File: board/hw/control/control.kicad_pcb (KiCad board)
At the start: 2 copper layers, 54.3 x 82.5 mm, 45 parts, among them J1 stepper #1, J2 stepper #2, J3 buttons, J4 power, J6 AVR-ISP-10, Q1 MMFTP84W, Q2 MMFTP84W, U1 ULN2003A, U2 ULN2003A, U3 ULN2003A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

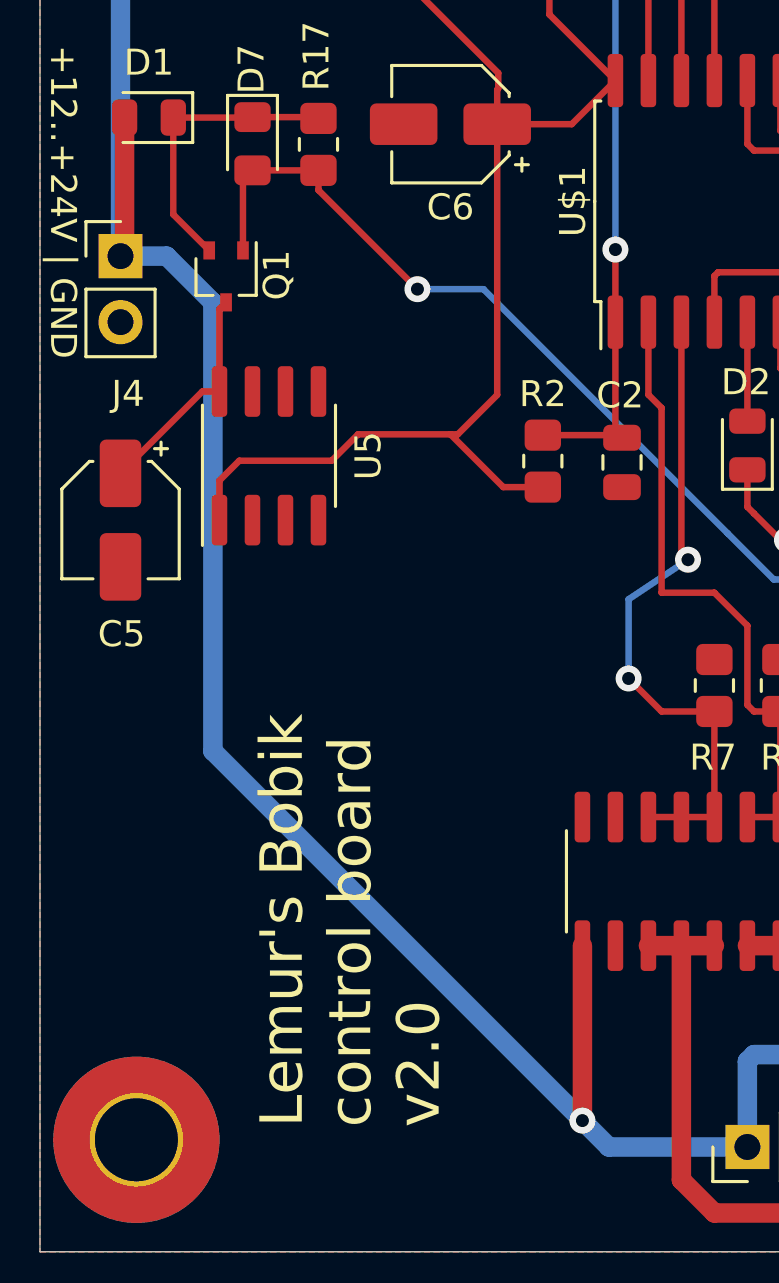
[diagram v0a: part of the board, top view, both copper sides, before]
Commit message: added power-on LED to +5V line
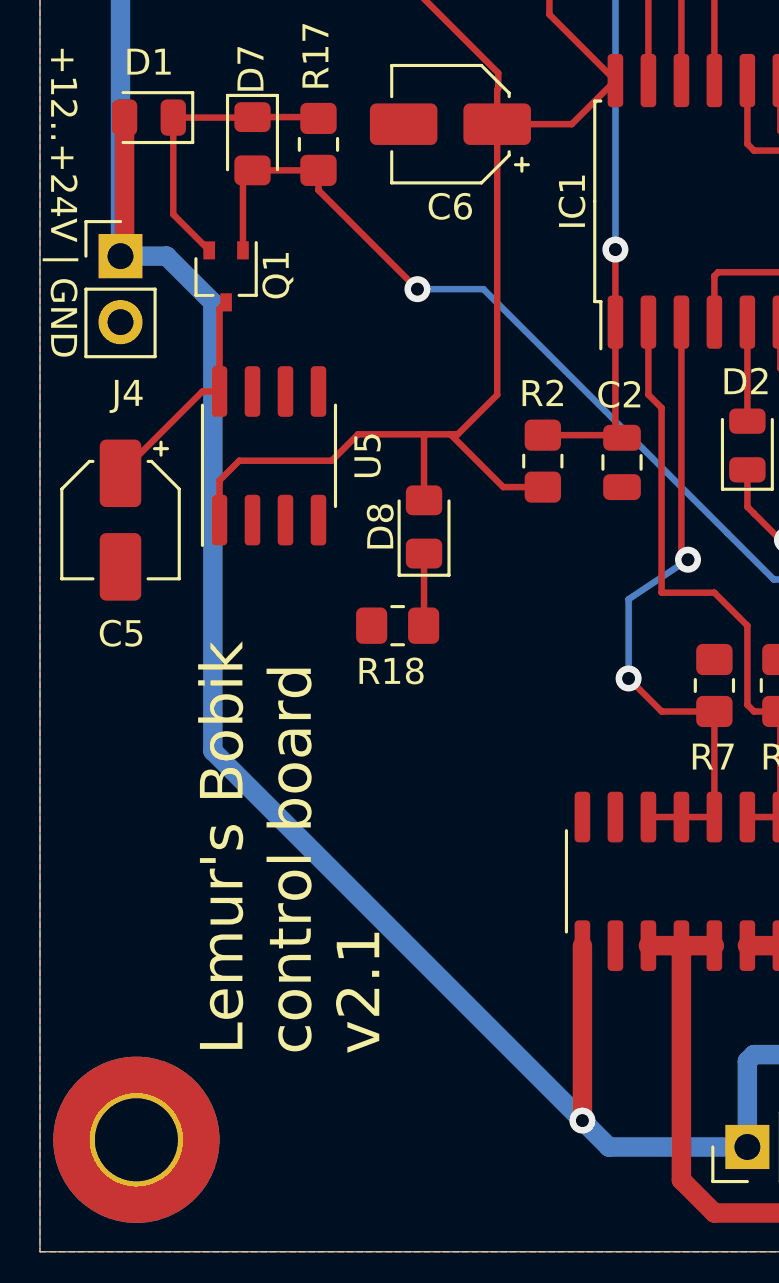
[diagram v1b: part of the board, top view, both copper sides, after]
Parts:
- added D8: LED green, LED_SMD:LED_0805_2012Metric_Pad1.15x1.40mm_HandSolder, F.Cu at (136.1, 118.4)
- added R18: 1kR, Resistor_SMD:R_0805_2012Metric_Pad1.20x1.40mm_HandSolder, F.Cu at (135.1, 122.2)
- renumbered U$1 to IC1
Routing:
- net Net-(D8-K): track 0.00 -> 2.78 mm
- net +5V: track 60.1 -> 62.7 mm
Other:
- board text added: "Lemur's Bobik control board v2.1"
- board text removed: "Lemur's Bobik control board v2.0"

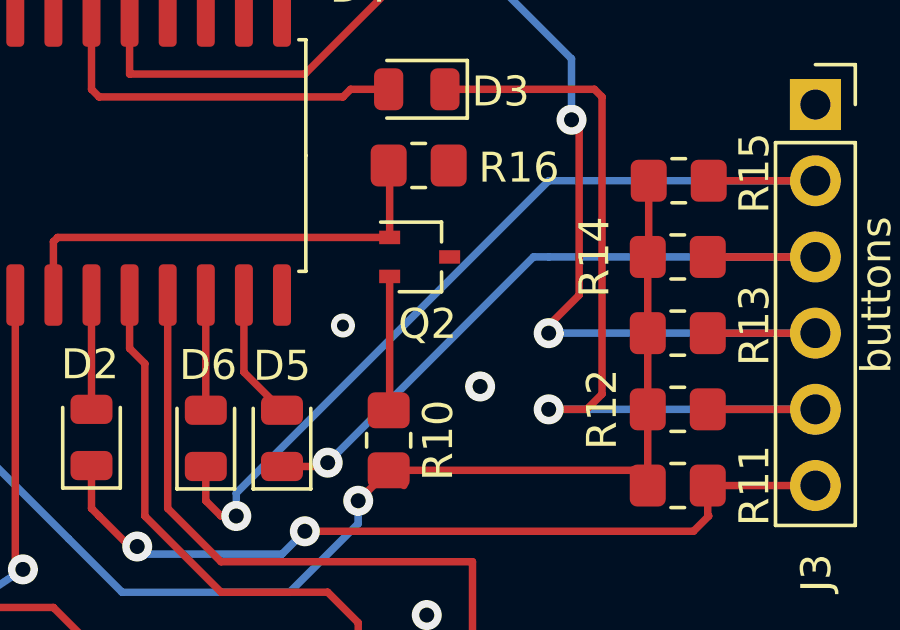
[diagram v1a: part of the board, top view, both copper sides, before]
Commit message: replaced P-MOSFET with N-MOSFET to maintain power-on state
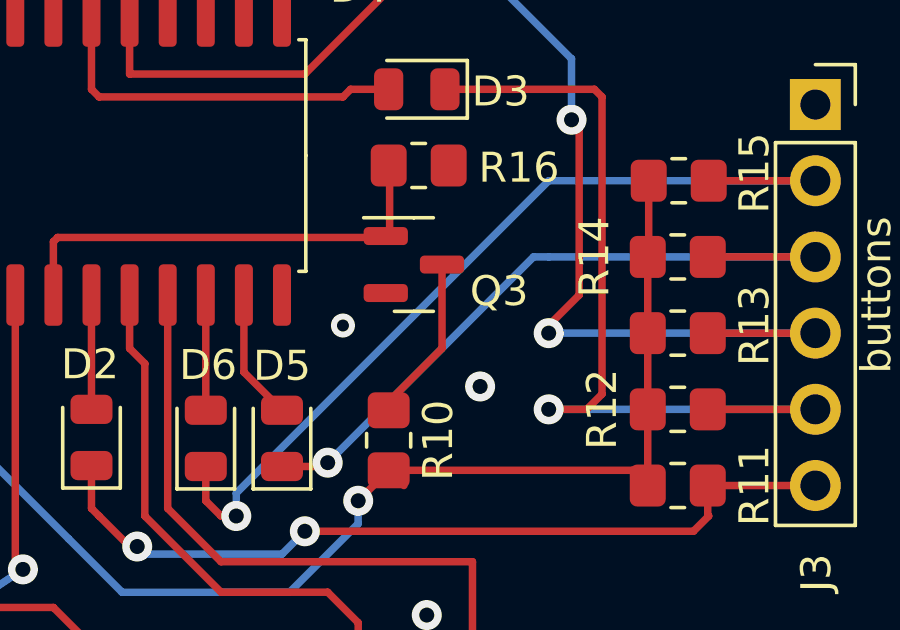
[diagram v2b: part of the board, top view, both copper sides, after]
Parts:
- removed Q2: MMFTP84W, Package_TO_SOT_SMD:SOT-323_SC-70
- added Q3: 2N7002, Package_TO_SOT_SMD:SOT-23, F.Cu at (159.3, 109.5)
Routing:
- net Net-(Q3-D): track 4.48 -> 5.64 mm

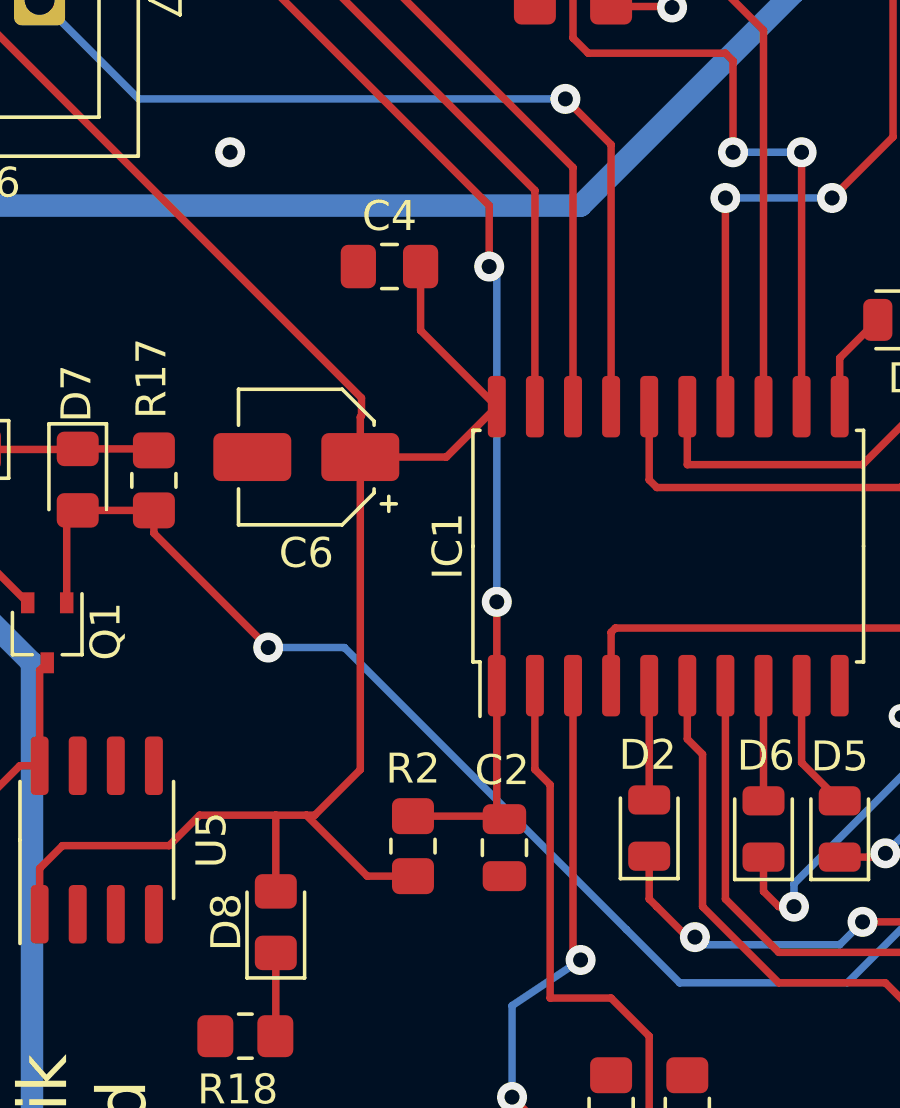
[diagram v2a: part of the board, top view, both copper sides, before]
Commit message: C2 and C4 are not 1206 as they should
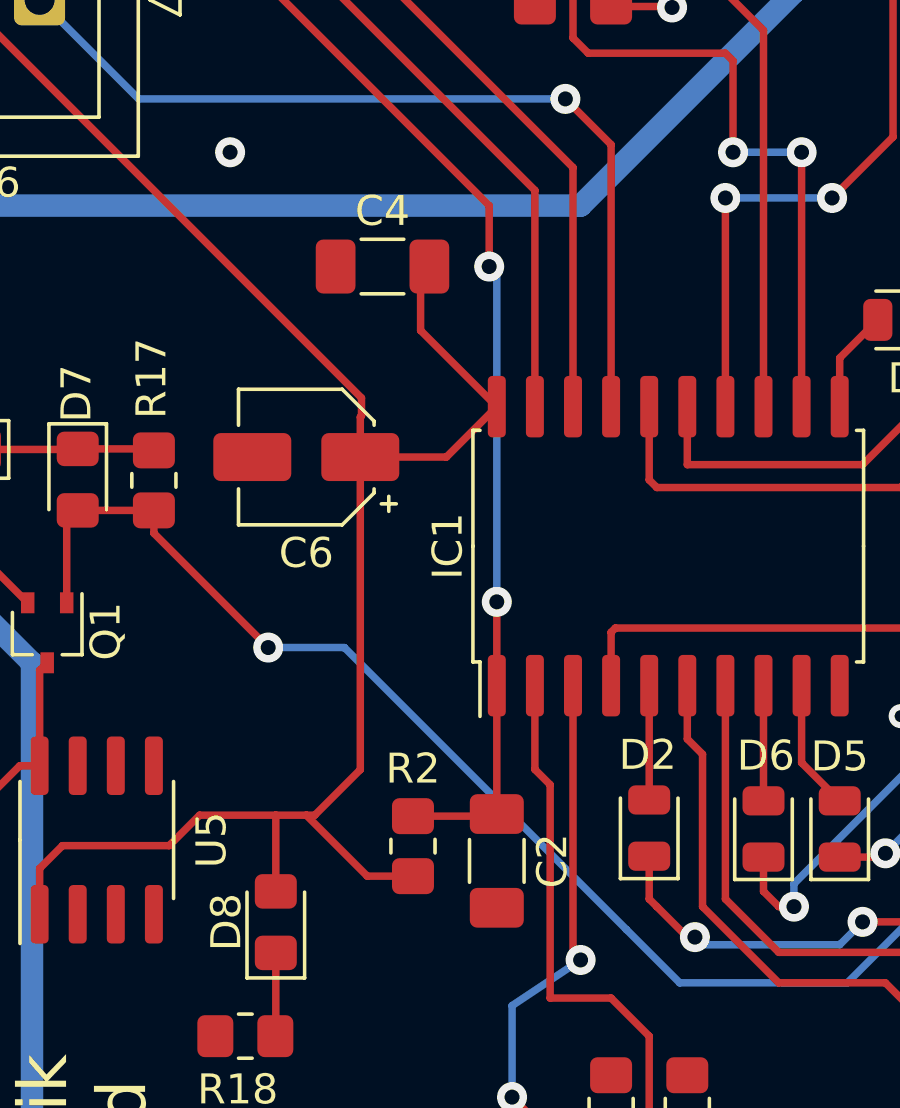
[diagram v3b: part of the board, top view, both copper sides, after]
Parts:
- C2: footprint Capacitor_SMD:C_0805_2012Metric -> Capacitor_SMD:C_1206_3216Metric_Pad1.33x1.80mm_HandSolder
- C4: footprint Capacitor_SMD:C_0805_2012Metric_Pad1.18x1.45mm_HandSolder -> Capacitor_SMD:C_1206_3216Metric_Pad1.33x1.80mm_HandSolder
- moved C2 0.51 mm to (143.5, 116.3)
- moved C4 0.23 mm to (139.7, 96.5)
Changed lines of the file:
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@@
     (pad "1" connect circle (at 0 0) (size 6.4 6.4) (layers "B.Cu" "B.Mask"))
   )
-  (footprint "Capacitor_SMD:C_0805_2012Metric" (layer "F.Cu")
-    (at 143.764 115.89 -90)
-    (descr "Capacitor SMD 0805 (2012 Metric), square (rectangular) end terminal, IPC_7351 nominal, (Body size source: IPC-SM-782 page 76, https://www.pcb-3d.com/wordpress/wp-content/uploads/ipc-sm-782a_amendment_1_and_2.pdf, https://docs.google.com/spreadsheets/d/1BsfQQcO9C6DZCsRaXUlFlo91Tg2WpOkGARC1WS5S8t0/edit?usp=sharing), generated with kicad-footprint-generator")
-    (tags "capacitor")
-    (property "Sheetfile" "control.kicad_sch")
-    (property "Sheetname" "")
-    (attr smd)
-    (fp_text reference "C2" (at -2.5806 0.0762 -180) (layer "F.SilkS")
-        (effects (font (size 1 1) (thickness 0.15)))
-    )
-    (fp_text value "100nF" (at 0 1.68 90) (layer "F.Fab")
-        (effects (font (size 1 1) (thickness 0.15)))
-    )
-    (fp_text user "${REFERENCE}" (at 0 0 90) (layer "F.Fab")
-        (effects (font (size 0.5 0.5) (thickness 0.08)))
-    )
-    (fp_line (start -0.261252 -0.735) (end 0.261252 -0.735)
-      (stroke (width 0.12) (type solid)) (layer "F.SilkS"))
-    (fp_line (start -0.261252 0.735) (end 0.261252 0.735)
-      (stroke (width 0.12) (type solid)) (layer "F.SilkS"))
-    (fp_line (start -1.7 -0.98) (end 1.7 -0.98)
-      (stroke (width 0.05) (type solid)) (layer "F.CrtYd"))
-    (fp_line (start -1.7 0.98) (end -1.7 -0.98)
-      (stroke (width 0.05) (type solid)) (layer "F.CrtYd"))
-    (fp_line (start 1.7 -0.98) (end 1.7 0.98)
-      (stroke (width 0.05) (type solid)) (layer "F.CrtYd"))
-    (fp_line (start 1.7 0.98) (end -1.7 0.98)
-      (stroke (width 0.05) (type solid)) (layer "F.CrtYd"))
-    (fp_line (start -1 -0.625) (end 1 -0.625)
-      (stroke (width 0.1) (type solid)) (layer "F.Fab"))
-    (fp_line (start -1 0.625) (end -1 -0.625)
-      (stroke (width 0.1) (type solid)) (layer "F.Fab"))
-    (fp_line (start 1 -0.625) (end 1 0.625)
-      (stroke (width 0.1) (type solid)) (layer "F.Fab"))
-    (fp_line (start 1 0.625) (end -1 0.625)
-      (stroke (width 0.1) (type solid)) (layer "F.Fab"))
-    (pad "1" smd roundrect (at -0.95 0 270) (size 1 1.45) (layers "F.Cu" "F.Paste" "F.Mask") (roundrect_rratio 0.25)
+  (footprint "Capacitor_SMD:C_1206_3216Metric_Pad1.33x1.80mm_HandSolder" (layer "F.Cu")
+    (at 143.51 116.332 -90)
+    (descr "Capacitor SMD 1206 (3216 Metric), square (rectangular) end terminal, IPC_7351 nominal with elongated pad for handsoldering. (Body size source: IPC-SM-782 page 76, https://www.pcb-3d.com/wordpress/wp-content/uploads/ipc-sm-782a_amendment_1_and_2.pdf), generated with kicad-footprint-generator")
+    (tags "capacitor handsolder")
+    (property "Sheetfile" "control.kicad_sch")
+    (property "Sheetname" "")
+    (attr smd)
+    (fp_text reference "C2" (at 0 -1.85 -90) (layer "F.SilkS")
+        (effects (font (size 1 1) (thickness 0.15)))
+    )
+    (fp_text value "100nF" (at 0 1.85 -90) (layer "F.Fab")
+        (effects (font (size 1 1) (thickness 0.15)))
+    )
+    (fp_text user "${REFERENCE}" (at 0 0 -90) (layer "F.Fab")
+        (effects (font (size 0.8 0.8) (thickness 0.12)))
+    )
+    (fp_line (start -0.711252 -0.91) (end 0.711252 -0.91)
+      (stroke (width 0.12) (type solid)) (layer "F.SilkS"))
+    (fp_line (start -0.711252 0.91) (end 0.711252 0.91)
+      (stroke (width 0.12) (type solid)) (layer "F.SilkS"))
+    (fp_line (start -2.48 -1.15) (end 2.48 -1.15)
+      (stroke (width 0.05) (type solid)) (layer "F.CrtYd"))
+    (fp_line (start -2.48 1.15) (end -2.48 -1.15)
+      (stroke (width 0.05) (type solid)) (layer "F.CrtYd"))
+    (fp_line (start 2.48 -1.15) (end 2.48 1.15)
+      (stroke (width 0.05) (type solid)) (layer "F.CrtYd"))
+    (fp_line (start 2.48 1.15) (end -2.48 1.15)
+      (stroke (width 0.05) (type solid)) (layer "F.CrtYd"))
+    (fp_line (start -1.6 -0.8) (end 1.6 -0.8)
+      (stroke (width 0.1) (type solid)) (layer "F.Fab"))
+    (fp_line (start -1.6 0.8) (end -1.6 -0.8)
+      (stroke (width 0.1) (type solid)) (layer "F.Fab"))
+    (fp_line (start 1.6 -0.8) (end 1.6 0.8)
+      (stroke (width 0.1) (type solid)) (layer "F.Fab"))
+    (fp_line (start 1.6 0.8) (end -1.6 0.8)
+      (stroke (width 0.1) (type solid)) (layer "F.Fab"))
+    (pad "1" smd roundrect (at -1.5625 0 270) (size 1.325 1.8) (layers "F.Cu" "F.Paste" "F.Mask") (roundrect_rratio 0.188679)
       (net 33 "Net-(IC1-PA2({slash}RESET))") (pinfunction "1") (pintype "passive"))
-    (pad "2" smd roundrect (at 0.95 0 270) (size 1 1.45) (layers "F.Cu" "F.Paste" "F.Mask") (roundrect_rratio 0.25)
+    (pad "2" smd roundrect (at 1.5625 0 270) (size 1.325 1.8) (layers "F.Cu" "F.Paste" "F.Mask") (roundrect_rratio 0.188679)
       (net 2 "0V") (pinfunction "2") (pintype "passive"))
-    (model "${KICAD6_3DMODEL_DIR}/Capacitor_SMD.3dshapes/C_0805_2012Metric.wrl"
+    (model "${KICAD6_3DMODEL_DIR}/Capacitor_SMD.3dshapes/C_1206_3216Metric.wrl"
       (offset (xyz 0 0 0))
       (scale (xyz 1 1 1))
@@
     )
   )
-  (footprint "Capacitor_SMD:C_0805_2012Metric_Pad1.18x1.45mm_HandSolder" (layer "F.Cu")
-    (at 139.9325 96.52)
-    (descr "Capacitor SMD 0805 (2012 Metric), square (rectangular) end terminal, IPC_7351 nominal with elongated pad for handsoldering. (Body size source: IPC-SM-782 page 76, https://www.pcb-3d.com/wordpress/wp-content/uploads/ipc-sm-782a_amendment_1_and_2.pdf, https://docs.google.com/spreadsheets/d/1BsfQQcO9C6DZCsRaXUlFlo91Tg2WpOkGARC1WS5S8t0/edit?usp=sharing), generated with kicad-footprint-generator")
+  (footprint "Capacitor_SMD:C_1206_3216Metric_Pad1.33x1.80mm_HandSolder" (layer "F.Cu")
+    (at 139.7 96.52)
+    (descr "Capacitor SMD 1206 (3216 Metric), square (rectangular) end terminal, IPC_7351 nominal with elongated pad for handsoldering. (Body size source: IPC-SM-782 page 76, https://www.pcb-3d.com/wordpress/wp-content/uploads/ipc-sm-782a_amendment_1_and_2.pdf), generated with kicad-footprint-generator")
     (tags "capacitor handsolder")
     (property "Sheetfile" "control.kicad_sch")
     (property "Sheetname" "")
     (attr smd)
-    (fp_text reference "C4" (at 0 -1.68) (layer "F.SilkS")
-        (effects (font (size 1 1) (thickness 0.15)))
-    )
-    (fp_text value "100nF" (at 0 1.68) (layer "F.Fab")
+    (fp_text reference "C4" (at 0 -1.85) (layer "F.SilkS")
+        (effects (font (size 1 1) (thickness 0.15)))
+    )
+    (fp_text value "100nF" (at 0 1.85) (layer "F.Fab")
         (effects (font (size 1 1) (thickness 0.15)))
     )
     (fp_text user "${REFERENCE}" (at 0 0) (layer "F.Fab")
-        (effects (font (size 0.5 0.5) (thickness 0.08)))
-    )
-    (fp_line (start -0.261252 -0.735) (end 0.261252 -0.735)
-      (stroke (width 0.12) (type solid)) (layer "F.SilkS"))
-    (fp_line (start -0.261252 0.735) (end 0.261252 0.735)
-      (stroke (width 0.12) (type solid)) (layer "F.SilkS"))
-    (fp_line (start -1.88 -0.98) (end 1.88 -0.98)
-      (stroke (width 0.05) (type solid)) (layer "F.CrtYd"))
-    (fp_line (start -1.88 0.98) (end -1.88 -0.98)
-      (stroke (width 0.05) (type solid)) (layer "F.CrtYd"))
-    (fp_line (start 1.88 -0.98) (end 1.88 0.98)
-      (stroke (width 0.05) (type solid)) (layer "F.CrtYd"))
-    (fp_line (start 1.88 0.98) (end -1.88 0.98)
-      (stroke (width 0.05) (type solid)) (layer "F.CrtYd"))
-    (fp_line (start -1 -0.625) (end 1 -0.625)
-      (stroke (width 0.1) (type solid)) (layer "F.Fab"))
-    (fp_line (start -1 0.625) (end -1 -0.625)
-      (stroke (width 0.1) (type solid)) (layer "F.Fab"))
-    (fp_line (start 1 -0.625) (end 1 0.625)
-      (stroke (width 0.1) (type solid)) (layer "F.Fab"))
-    (fp_line (start 1 0.625) (end -1 0.625)
-      (stroke (width 0.1) (type solid)) (layer "F.Fab"))
-    (pad "1" smd roundrect (at -1.0375 0) (size 1.175 1.45) (layers "F.Cu" "F.Paste" "F.Mask") (roundrect_rratio 0.212766)
+        (effects (font (size 0.8 0.8) (thickness 0.12)))
+    )
+    (fp_line (start -0.711252 -0.91) (end 0.711252 -0.91)
+      (stroke (width 0.12) (type solid)) (layer "F.SilkS"))
+    (fp_line (start -0.711252 0.91) (end 0.711252 0.91)
+      (stroke (width 0.12) (type solid)) (layer "F.SilkS"))
+    (fp_line (start -2.48 -1.15) (end 2.48 -1.15)
+      (stroke (width 0.05) (type solid)) (layer "F.CrtYd"))
+    (fp_line (start -2.48 1.15) (end -2.48 -1.15)
+      (stroke (width 0.05) (type solid)) (layer "F.CrtYd"))
+    (fp_line (start 2.48 -1.15) (end 2.48 1.15)
+      (stroke (width 0.05) (type solid)) (layer "F.CrtYd"))
+    (fp_line (start 2.48 1.15) (end -2.48 1.15)
+      (stroke (width 0.05) (type solid)) (layer "F.CrtYd"))
+    (fp_line (start -1.6 -0.8) (end 1.6 -0.8)
+      (stroke (width 0.1) (type solid)) (layer "F.Fab"))
+    (fp_line (start -1.6 0.8) (end -1.6 -0.8)
+      (stroke (width 0.1) (type solid)) (layer "F.Fab"))
+    (fp_line (start 1.6 -0.8) (end 1.6 0.8)
+      (stroke (width 0.1) (type solid)) (layer "F.Fab"))
+    (fp_line (start 1.6 0.8) (end -1.6 0.8)
+      (stroke (width 0.1) (type solid)) (layer "F.Fab"))
+    (pad "1" smd roundrect (at -1.5625 0) (size 1.325 1.8) (layers "F.Cu" "F.Paste" "F.Mask") (roundrect_rratio 0.188679)
       (net 2 "0V") (pinfunction "1") (pintype "passive"))
-    (pad "2" smd roundrect (at 1.0375 0) (size 1.175 1.45) (layers "F.Cu" "F.Paste" "F.Mask") (roundrect_rratio 0.212766)
+    (pad "2" smd roundrect (at 1.5625 0) (size 1.325 1.8) (layers "F.Cu" "F.Paste" "F.Mask") (roundrect_rratio 0.188679)
       (net 1 "+5V") (pinfunction "2") (pintype "passive"))
-    (model "${KICAD6_3DMODEL_DIR}/Capacitor_SMD.3dshapes/C_0805_2012Metric.wrl"
-      (offset (xyz 0 0 0))
-      (scale (xyz 1 1 1))
+    (model "${KICAD6_3DMODEL_DIR}/Capacitor_SMD.3dshapes/C_1206_3216Metric.wrl"
+      (offset (xyz 0 0 0))
+      (scale (xyz 1 1 1))
